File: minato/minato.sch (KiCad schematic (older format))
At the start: 209 parts, among them U1 Elite-C

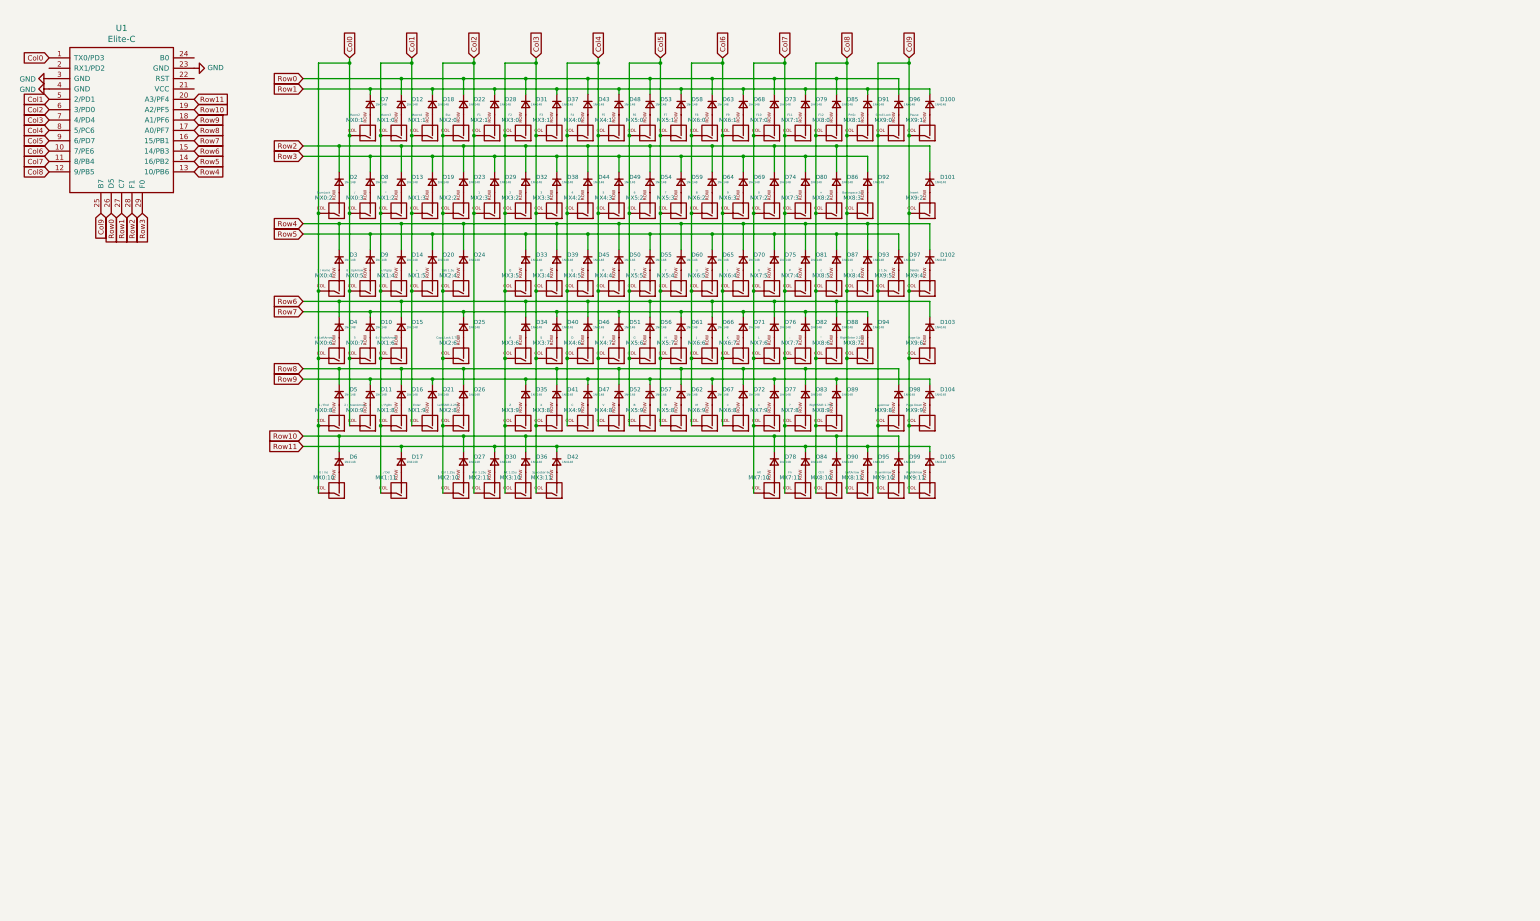
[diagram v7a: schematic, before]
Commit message: :construction: Add STM32F103 schematic
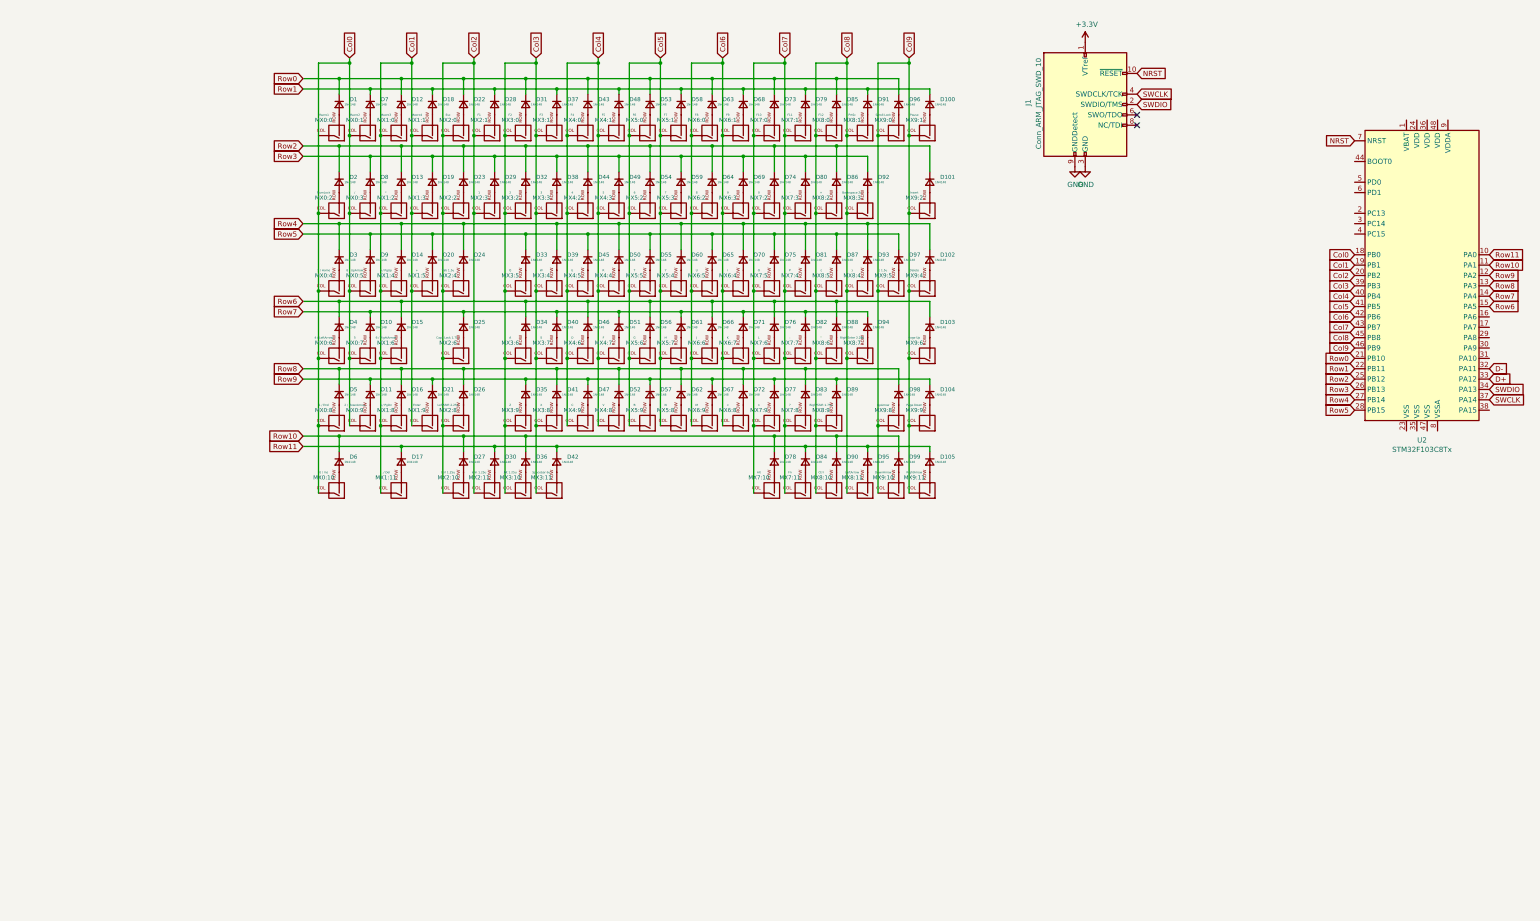
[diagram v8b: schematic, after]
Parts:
- removed U1: Elite-C, Keebio-Parts.pretty:Elite-C-castellated-29pin, symbol keebio-components:Elite-C
- added D1: 1N4148, Diode_SMD:D_SOD-123, symbol Device:D_Small
- added J1: Conn_ARM_JTAG_SWD_10, symbol Connector:Conn_ARM_JTAG_SWD_10
- added MX0:0: Macro1, keyswitches.pretty:Kailh_socket_MX, symbol MX_Alps_Hybrid:MX-NoLED
- added U2: STM32F103C8Tx, Package_QFP:LQFP-48_7x7mm_P0.5mm, symbol MCU_ST_STM32F1:STM32F103C8Tx
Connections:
- net Col0: now also U2.18 (PB0)
- net Col1: now also U2.19 (PB1)
- net Col2: now also U2.20 (PB2)
- net Col3: now also U2.39 (PB3)
- net Col4: now also U2.40 (PB4)
- net Col5: now also U2.41 (PB5)
- net Col6: now also U2.42 (PB6)
- net Col7: now also U2.43 (PB7)
- net Col8: now also U2.45 (PB8)
- net Col9: now also U2.46 (PB9)
- net GND: now also J1.3 (GND), J1.5 (GND), J1.9 (GNDDetect)
- net Row0: now also D1.1 (K), U2.21 (PB10)
- net Row1: now also U2.22 (PB11)
- net Row10: now also U2.11 (PA1)
- net Row11: now also U2.10 (PA0)
- net Row2: now also U2.25 (PB12)
- net Row3: now also U2.26 (PB13)
- net Row4: now also U2.27 (PB14)
- net Row5: now also U2.28 (PB15)
- net Row6: now also U2.15 (PA5)
- net Row7: now also U2.14 (PA4)
- net Row8: now also U2.13 (PA3)
- net Row9: now also U2.12 (PA2)
- new net: D1.2 (A), MX0:0.2 (ROW)
- new net +3V3: J1.1 (VTref)
- new net D+: U2.33 (PA12)
- new net D-: U2.32 (PA11)
- new net NRST: J1.10 (~RESET~), U2.7 (NRST)
- new net SWCLK: J1.4 (SWDCLK/TCK), U2.37 (PA14)
- new net SWDIO: J1.2 (SWDIO/TMS), U2.34 (PA13)
- no-connect marks 0 -> 2
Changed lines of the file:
@@
 Comment4 ""
 $EndDescr
-$Comp
-L keebio-components:Elite-C U1
-U 1 1 5E3DD7C7
-P 1550 1500
-F 0 "U1" H 1550 2337 60  0000 C CNN
-F 1 "Elite-C" H 1550 2231 60  0000 C CNN
-F 2 "Keebio-Parts.pretty:Elite-C-castellated-29pin" V 2600 -1000 60  0001 C CNN
-F 3 "" V 2600 -1000 60  0001 C CNN
-	1    1550 1500
-	1    0    0    -1
-$EndComp
-Text GLabel 850  950  0    50   Input ~ 0
+Text GLabel 13450 2850 0    50   Input ~ 0
 Col0
-Text GLabel 850  1350 0    50   Input ~ 0
+Text GLabel 13450 2950 0    50   Input ~ 0
 Col1
-Text GLabel 850  1450 0    50   Input ~ 0
+Text GLabel 13450 3050 0    50   Input ~ 0
 Col2
-Text GLabel 850  1550 0    50   Input ~ 0
+Text GLabel 13450 3150 0    50   Input ~ 0
 Col3
-Text GLabel 850  1650 0    50   Input ~ 0
+Text GLabel 13450 3250 0    50   Input ~ 0
 Col4
-Text GLabel 850  1750 0    50   Input ~ 0
+Text GLabel 13450 3350 0    50   Input ~ 0
 Col5
-Text GLabel 850  1850 0    50   Input ~ 0
+Text GLabel 13450 3450 0    50   Input ~ 0
 Col6
 Text GLabel 3300 1250 0    50   Input ~ 0
@@
 Wire Wire Line
 	9350 4750 9350 4700
-Text GLabel 850  1950 0    50   Input ~ 0
+Text GLabel 13450 3550 0    50   Input ~ 0
 Col7
-Text GLabel 850  2050 0    50   Input ~ 0
+Text GLabel 13450 3650 0    50   Input ~ 0
 Col8
-Text GLabel 1350 2450 3    50   Input ~ 0
+Text GLabel 13450 3750 0    50   Input ~ 0
 Col9
-Text GLabel 1450 2450 3    50   Input ~ 0
+Text GLabel 13450 3850 0    50   Input ~ 0
 Row0
-Text GLabel 1550 2450 3    50   Input ~ 0
+Text GLabel 13450 3950 0    50   Input ~ 0
 Row1
-Text GLabel 1650 2450 3    50   Input ~ 0
+Text GLabel 13450 4050 0    50   Input ~ 0
 Row2
-Text GLabel 1750 2450 3    50   Input ~ 0
+Text GLabel 13450 4150 0    50   Input ~ 0
 Row3
-Text GLabel 2250 2050 2    50   Input ~ 0
+Text GLabel 13450 4250 0    50   Input ~ 0
 Row4
-Text GLabel 2250 1950 2    50   Input ~ 0
+Text GLabel 13450 4350 0    50   Input ~ 0
 Row5
-Text GLabel 2250 1850 2    50   Input ~ 0
+Text GLabel 14750 3350 2    50   Input ~ 0
 Row6
-Text GLabel 2250 1750 2    50   Input ~ 0
+Text GLabel 14750 3250 2    50   Input ~ 0
 Row7
-Text GLabel 2250 1650 2    50   Input ~ 0
-Row8
-Text GLabel 2250 1550 2    50   Input ~ 0
+Text GLabel 14750 3050 2    50   Input ~ 0
 Row9
-Text GLabel 2250 1450 2    50   Input ~ 0
+Text GLabel 14750 2950 2    50   Input ~ 0
 Row10
-Text GLabel 2250 1350 2    50   Input ~ 0
+Text GLabel 14750 2850 2    50   Input ~ 0
 Row11
 $Comp
@@
 Wire Wire Line
 	3950 1250 4550 1250
-Wire Wire Line
-	3300 1250 3950 1250
 Connection ~ 3950 1250
 Wire Wire Line
@@
 	3450 1000 3450 2450
 Wire Wire Line
-	3300 1150 4250 1150
+	3300 1150 3650 1150
 $Comp
-L power:GND #PWR?
-U 1 1 5E57B2BC
-P 850 1250
-F 0 "#PWR?" H 850 1000 50  0001 C CNN
-F 1 "GND" V 855 1122 50  0000 R CNN
-F 2 "" H 850 1250 50  0001 C CNN
-F 3 "" H 850 1250 50  0001 C CNN
-	1    850  1250
-	0    1    1    0
+L MCU_ST_STM32F1:STM32F103C8Tx U2
+U 1 1 5E445AE3
+P 14150 3050
+F 0 "U2" H 14100 1461 50  0000 C CNN
+F 1 "STM32F103C8Tx" H 14100 1370 50  0000 C CNN
+F 2 "Package_QFP:LQFP-48_7x7mm_P0.5mm" H 13550 1650 50  0001 R CNN
+F 3 "http://www.st.com/st-web-ui/static/active/en/resource/technical/document/datasheet/CD00161566.pdf" H 14150 3050 50  0001 C CNN
+	1    14150 3050
+	1    0    0    -1
 $EndComp
 $Comp
-L power:GND #PWR?
-U 1 1 5E57CB9D
-P 2250 1050
-F 0 "#PWR?" H 2250 800 50  0001 C CNN
-F 1 "GND" V 2255 922 50  0000 R CNN
-F 2 "" H 2250 1050 50  0001 C CNN
-F 3 "" H 2250 1050 50  0001 C CNN
-	1    2250 1050
-	0    -1   -1   0
-$EndComp
-$Comp
-L power:GND #PWR?
-U 1 1 5E57DFD0
-P 850 1150
-F 0 "#PWR?" H 850 900 50  0001 C CNN
-F 1 "GND" V 855 1022 50  0000 R CNN
-F 2 "" H 850 1150 50  0001 C CNN
-F 3 "" H 850 1150 50  0001 C CNN
-	1    850  1150
+L Device:D_Small D1
+U 1 1 5E46D07D
+P 3650 1400
+F 0 "D1" V 3600 1500 39  0000 L CNN
+F 1 "1N4148" V 3650 1450 20  0000 L CNN
+F 2 "Diode_SMD:D_SOD-123" V 3650 1400 50  0001 C CNN
+F 3 "~" V 3650 1400 50  0001 C CNN
+	1    3650 1400
 	0    1    1    0
 $EndComp
+$Comp
+L MX_Alps_Hybrid:MX-NoLED MX0:0
+U 1 1 5E46D083
+P 3600 1650
+F 0 "MX0:0" H 3700 1550 39  0000 C CNN
+F 1 "Macro1" H 3700 1500 20  0000 C CNN
+F 2 "keyswitches.pretty:Kailh_socket_MX" H 2975 1625 60  0001 C CNN
+F 3 "" H 2975 1625 60  0001 C CNN
+	1    3600 1650
+	-1   0    0    1
+$EndComp
+Text GLabel 14750 3150 2    50   Input ~ 0
+Row8
+$Comp
+L Connector:Conn_ARM_JTAG_SWD_10 J1
+U 1 1 5E479C5D
+P 10850 1400
+F 0 "J1" V 10300 1450 50  0000 R CNN
+F 1 "Conn_ARM_JTAG_SWD_10" V 10400 1850 50  0000 R CNN
+F 2 "" H 10850 1400 50  0001 C CNN
+F 3 "http://infocenter.arm.com/help/topic/com.arm.doc.ddi0314h/DDI0314H_coresight_components_trm.pdf" V 10500 150 50  0001 C CNN
+	1    10850 1400
+	1    0    0    -1
+$EndComp
+$Comp
+L power:GND #PWR0101
+U 1 1 5E47FDAE
+P 10750 2000
+F 0 "#PWR0101" H 10750 1750 50  0001 C CNN
+F 1 "GND" H 10755 1827 50  0000 C CNN
+F 2 "" H 10750 2000 50  0001 C CNN
+F 3 "" H 10750 2000 50  0001 C CNN
+	1    10750 2000
+	1    0    0    -1
+$EndComp
+$Comp
+L power:GND #PWR0102
+U 1 1 5E481769
+P 10850 2000
+F 0 "#PWR0102" H 10850 1750 50  0001 C CNN
+F 1 "GND" H 10855 1827 50  0000 C CNN
+F 2 "" H 10850 2000 50  0001 C CNN
+F 3 "" H 10850 2000 50  0001 C CNN
+	1    10850 2000
+	1    0    0    -1
+$EndComp
+$Comp
+L power:+3.3V #PWR0103
+U 1 1 5E483BED
+P 10850 800
+F 0 "#PWR0103" H 10850 650 50  0001 C CNN
+F 1 "+3.3V" H 10865 973 50  0000 C CNN
+F 2 "" H 10850 800 50  0001 C CNN
+F 3 "" H 10850 800 50  0001 C CNN
+	1    10850 800
+	1    0    0    -1
+$EndComp
+Text GLabel 11350 1100 2    50   Input ~ 0
+NRST
+Text GLabel 11350 1300 2    50   Input ~ 0
+SWCLK
+Text GLabel 11350 1400 2    50   Input ~ 0
+SWDIO
+NoConn ~ 11350 1500
+NoConn ~ 11350 1600
+Text GLabel 13450 1750 0    50   Input ~ 0
+NRST
+Text GLabel 14750 4050 2    50   Input ~ 0
+D+
+Text GLabel 14750 3950 2    50   Input ~ 0
+D-
+Text GLabel 14750 4150 2    50   Input ~ 0
+SWDIO
+Text GLabel 14750 4250 2    50   Input ~ 0
+SWCLK
+Wire Wire Line
+	3300 1250 3950 1250
+Wire Wire Line
+	3650 1300 3650 1150
+Connection ~ 3650 1150
+Wire Wire Line
+	3650 1150 4250 1150
 $EndSCHEMATC
